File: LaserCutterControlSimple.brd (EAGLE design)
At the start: 75.9 x 53.3 mm, 31 parts, among them J4 FAN, J5 AIR, J6 E-STOP, J7 04-JST-B4B-XH-A, Q1 FDN5630, Q2 FDN5630, U3 R1SE-0505, Y2 POLOLU_A4988, Y3 POLOLU_A4988

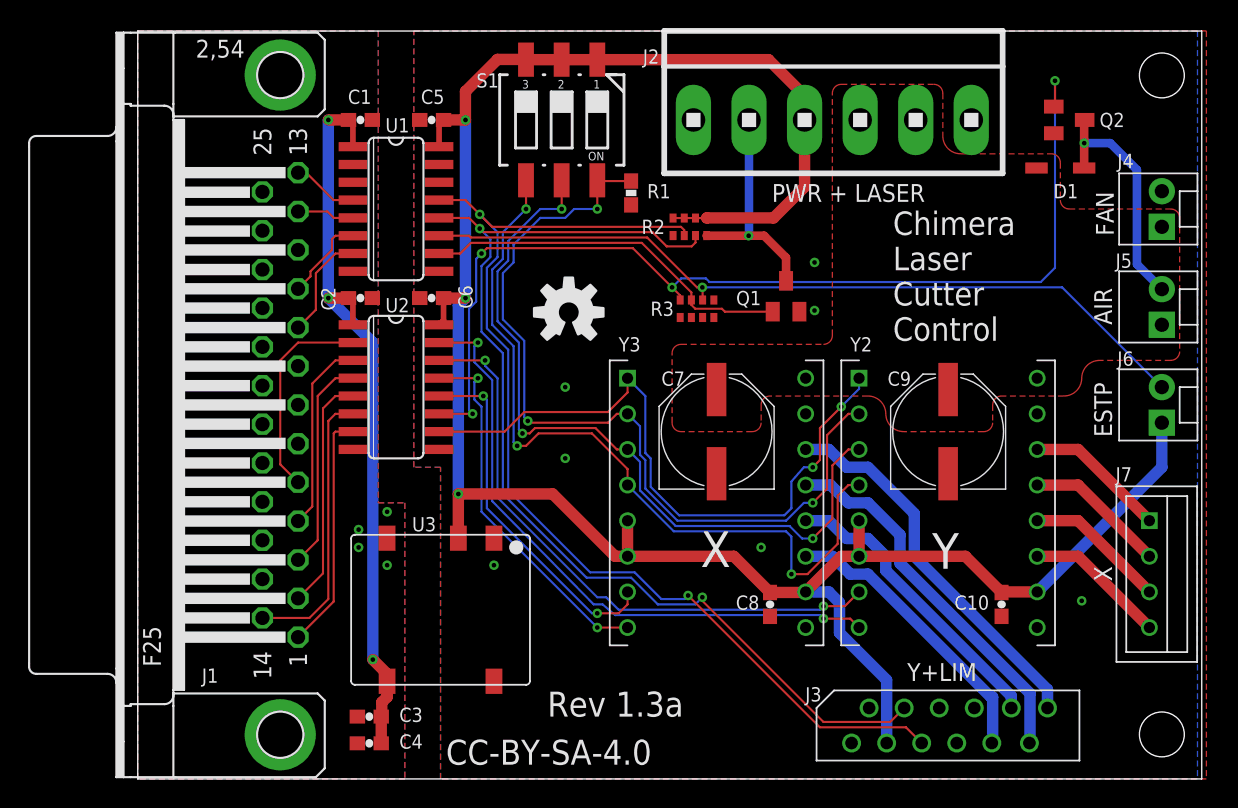
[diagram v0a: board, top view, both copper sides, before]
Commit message: Minor dumb change because it was very early in the morning when I finished the simplified board design. Silk screen and connector change to better match laser cutter connections.
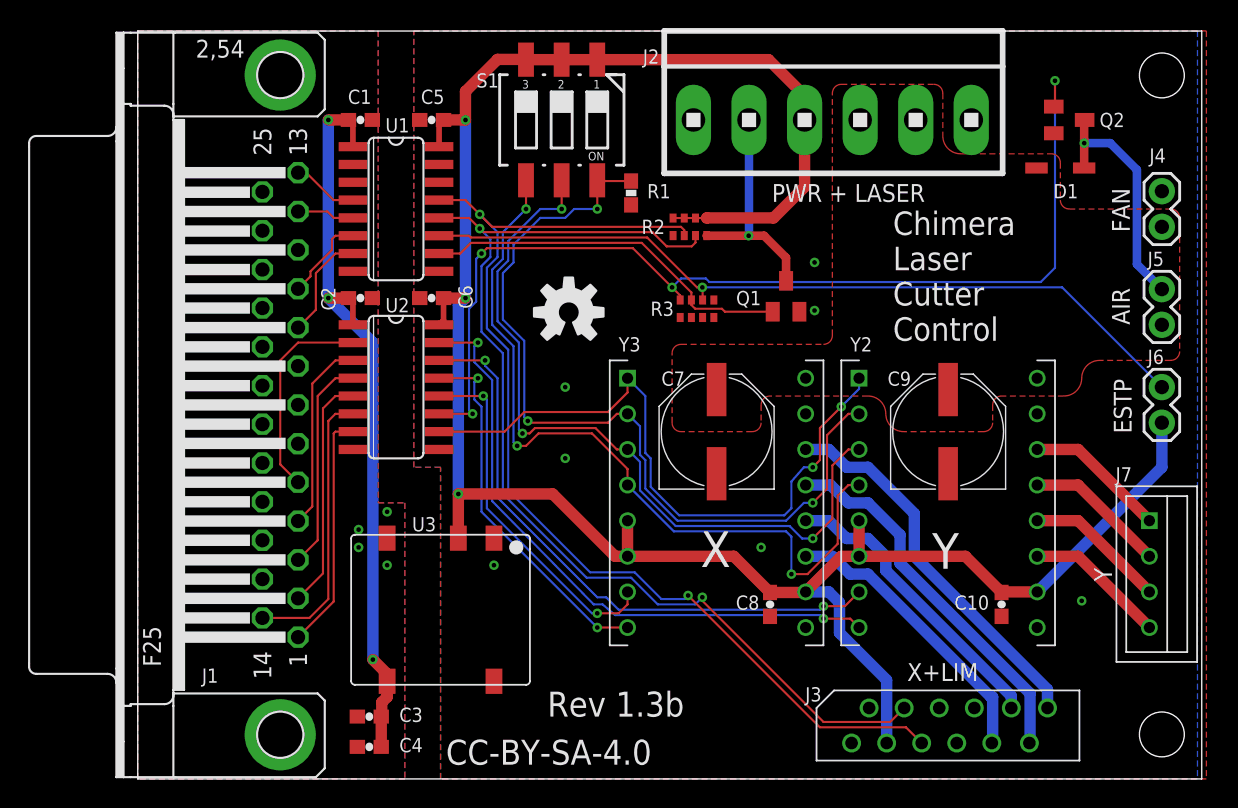
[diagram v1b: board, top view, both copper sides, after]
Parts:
- J4, J5, J6: device SparkFun-Connectors:MOLEX-1X2 -> SparkFun-Connectors:1X02
- moved C4 0.25 mm to (16.5, 2.29)
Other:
- board text added: "Rev 1.3b"
- board text added: "X+LIM"
- board text removed: "Rev 1.3a"
- board text removed: "Y+LIM"
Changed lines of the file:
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@@
 <hole x="73.025" y="50.165" drill="3.2"/>
 <hole x="73.025" y="3.175" drill="3.2"/>
-<text x="69.469" y="32.385" size="1.27" layer="21" font="vector" ratio="12" rot="R90">AIR</text>
-<text x="69.469" y="24.384" size="1.27" layer="21" font="vector" ratio="12" rot="R90">ESTP</text>
-<text x="69.469" y="14.097" size="1.27" layer="21" font="vector" ratio="12" rot="R90">X</text>
-<text x="69.596" y="38.735" size="1.27" layer="21" font="vector" ratio="12" rot="R90">FAN</text>
-<text x="54.864" y="6.985" size="1.27" layer="21" font="vector" ratio="12">Y+LIM</text>
+<text x="70.739" y="32.385" size="1.27" layer="21" font="vector" ratio="12" rot="R90">AIR</text>
+<text x="70.866" y="24.638" size="1.27" layer="21" font="vector" ratio="12" rot="R90">ESTP</text>
+<text x="69.469" y="14.097" size="1.27" layer="21" font="vector" ratio="12" rot="R90">Y</text>
+<text x="70.739" y="38.989" size="1.27" layer="21" font="vector" ratio="12" rot="R90">FAN</text>
+<text x="54.864" y="6.985" size="1.27" layer="21" font="vector" ratio="12">X+LIM</text>
 <text x="53.848" y="31.242" size="1.6764" layer="21" font="vector" ratio="15">Chimera
 Laser
 Cutter
 Control</text>
-<text x="69.85" y="43.561" size="1.016" layer="21" font="vector" ratio="12">J4</text>
-<text x="69.723" y="36.449" size="1.016" layer="21" font="vector" ratio="12">J5</text>
-<text x="69.85" y="29.464" size="1.016" layer="21" font="vector" ratio="12">J6</text>
+<text x="72.136" y="43.942" size="1.016" layer="21" font="vector" ratio="12">J4</text>
+<text x="72.009" y="36.576" size="1.016" layer="21" font="vector" ratio="12">J5</text>
+<text x="72.009" y="29.591" size="1.016" layer="21" font="vector" ratio="12">J6</text>
 <text x="56.134" y="42.418" size="1.27" layer="21" font="vector" ratio="12" rot="R180">PWR + LASER</text>
 <text x="40.132" y="15.113" size="2.54" layer="21" font="vector" ratio="15">X</text>
 <text x="56.642" y="14.986" size="2.54" layer="21" font="vector" ratio="15">Y</text>
 <text x="21.971" y="1.016" size="1.778" layer="21" font="vector" ratio="12">CC-BY-SA-4.0</text>
-<text x="29.21" y="4.445" size="1.778" layer="21" font="vector" ratio="12">Rev 1.3a</text>
+<text x="29.21" y="4.445" size="1.778" layer="21" font="vector" ratio="12">Rev 1.3b</text>
 </plain>
 <attributes>
@@
 <attribute name="VALUE" x="17.526" y="5.588" size="0.4064" layer="27" font="vector" rot="R180" display="off"/>
 </element>
-<element name="C4" library="SparkFun-Capacitors" package="0603-CAP" value="2.2uF" x="16.51" y="2.54" locked="yes" smashed="yes" rot="R180">
-<attribute name="PROD_ID" value="CAP-07886" x="16.51" y="2.54" size="1.778" layer="27" rot="R180" display="off"/>
-<attribute name="NAME" x="20.32" y="3.175" size="1.016" layer="25" font="vector" ratio="12" rot="R180"/>
-<attribute name="VALUE" x="17.526" y="3.683" size="0.4064" layer="27" font="vector" rot="R180" display="off"/>
+<element name="C4" library="SparkFun-Capacitors" package="0603-CAP" value="2.2uF" x="16.51" y="2.286" smashed="yes" rot="R180">
+<attribute name="PROD_ID" value="CAP-07886" x="16.51" y="2.286" size="1.778" layer="27" rot="R180" display="off"/>
+<attribute name="NAME" x="20.32" y="2.921" size="1.016" layer="25" font="vector" ratio="12" rot="R180"/>
+<attribute name="VALUE" x="17.526" y="3.429" size="0.4064" layer="27" font="vector" rot="R180" display="off"/>
 </element>
 <element name="C5" library="SparkFun-Capacitors" package="0603-CAP" value="1nF" x="20.955" y="46.99" locked="yes" smashed="yes" rot="R180">
@@
 <attribute name="VALUE" x="-3.81" y="18.288" size="1.778" layer="27" ratio="10" rot="R90"/>
 </element>
-<element name="J4" library="SparkFun-Connectors" package="MOLEX-1X2" value="FAN" x="73.025" y="39.37" locked="yes" smashed="yes" rot="R90"/>
-<element name="J6" library="SparkFun-Connectors" package="MOLEX-1X2" value="E-STOP" x="73.025" y="25.4" locked="yes" smashed="yes" rot="R90"/>
+<element name="J4" library="SparkFun-Connectors" package="1X02" value="FAN" x="73.025" y="39.37" locked="yes" smashed="yes" rot="R90"/>
+<element name="J6" library="SparkFun-Connectors" package="1X02" value="E-STOP" x="73.025" y="25.4" locked="yes" smashed="yes" rot="R90"/>
 <element name="J3" library="con-amp-te" package="12P" value="" x="57.15" y="3.81" locked="yes" smashed="yes">
 <attribute name="OC_NEWARK" value="unknown" x="57.15" y="3.81" size="1.778" layer="27" display="off"/>
@@
 <attribute name="VALUE" x="38.1351" y="51.3408" size="1.27" layer="27"/>
 </element>
-<element name="J5" library="SparkFun-Connectors" package="MOLEX-1X2" value="AIR" x="73.025" y="32.385" locked="yes" smashed="yes" rot="R90"/>
+<element name="J5" library="SparkFun-Connectors" package="1X02" value="AIR" x="73.025" y="32.385" locked="yes" smashed="yes" rot="R90"/>
 <element name="LOGO1" library="SparkFun-Aesthetics" package="OSHW-LOGO-M" value="OSHW-LOGOM" x="30.734" y="33.274"/>
 <element name="Q2" library="Fairchild_By_element14_Batch_1" package="SOT23" value="FDN5630" x="66.421" y="46.99" locked="yes" smashed="yes" rot="R270">
@@
 <element name="U1" library="silicon-labs" package="SO16" value="" x="18.415" y="40.64" locked="yes" smashed="yes" rot="R270">
 <attribute name="VALUE" x="17.78" y="44.704" size="1.27" layer="27" ratio="10" rot="R270"/>
-<attribute name="NAME" x="17.653" y="46.101" size="1.016" layer="25" font="vector"/>
+<attribute name="NAME" x="17.653" y="46.101" size="1.016" layer="25" font="vector" ratio="12"/>
 </element>
 <element name="U2" library="silicon-labs" package="SO16" value="" x="18.415" y="27.94" locked="yes" smashed="yes" rot="R270">
@@
 <wire x1="17.399" y1="5.461" x2="17.399" y2="4.484" width="0.8128" layer="1"/>
 <wire x1="17.399" y1="4.484" x2="17.36" y2="4.445" width="0.8128" layer="1"/>
-<wire x1="17.36" y1="4.445" x2="17.36" y2="2.54" width="0.8128" layer="1"/>
+<wire x1="17.36" y1="4.445" x2="17.36" y2="2.286" width="0.8128" layer="1"/>
 <wire x1="17.78" y1="6.965" x2="17.78" y2="7.493" width="0.8128" layer="1"/>
 <wire x1="17.78" y1="7.493" x2="16.764" y2="8.509" width="0.8128" layer="1"/>

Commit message: More tweaks to 1.3-1 and 1.3b, some repositioning and swapping of parts for layout, now that I've seen what the inside of the laser cutter looks like. Added pinouts for X and Y limits to the simple board, and just now realize I might have problems with the digital isolators being one way only...
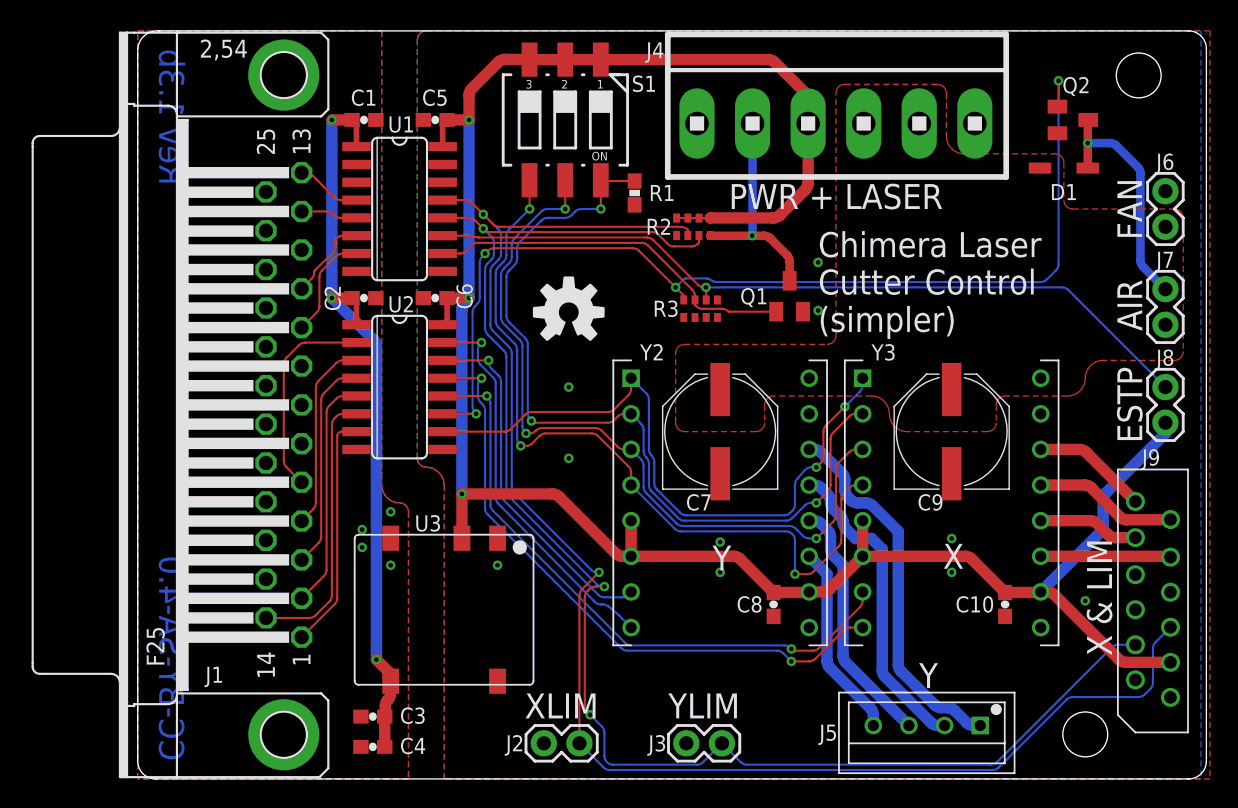
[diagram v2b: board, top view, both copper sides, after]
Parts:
- added J8: E-STOP, SparkFun-Connectors:1X02
- added J9: (no value), con-amp-te:12P
- J2: value (none) -> XLIM; device con-amp:1X6MTA -> SparkFun-Connectors:1X02
- J3: value (none) -> YLIM; device con-amp-te:12P -> SparkFun-Connectors:1X02
- J4: value FAN -> (none); device SparkFun-Connectors:1X02 -> con-amp:1X6MTA
- J5: value AIR -> 04-JST-B4B-XH-A; device SparkFun-Connectors:1X02 -> con-jst-xh:B4B-XH
- J6: value E-STOP -> FAN
- J7: value 04-JST-B4B-XH-A -> AIR; device con-jst-xh:B4B-XH -> SparkFun-Connectors:1X02
- moved J2 49.0 mm to (29.0, 2.54)
- moved J5 33.1 mm to (56.3, 3.81), turned to 180 degrees
- moved J4 24.4 mm to (49.8, 46.7), turned to 0 degrees
- moved J3 18.1 mm to (39.1, 2.54)
- moved J7 17.8 mm to (73.3, 32.4), turned to 90 degrees
- moved Y3 16.8 mm to (58.0, 19.7)
- moved Y2 16.3 mm to (41.5, 19.7)
- moved J6 14.0 mm to (73.3, 39.4)
- moved C7 0.25 mm to (41.5, 24.8)
- moved C9 0.25 mm to (58.0, 24.8)
- moved D1 0.25 mm to (66.0, 43.6)
- moved R2 0.25 mm to (39.6, 39.4)
- moved C1 0.25 mm to (16.1, 47.0)
- moved C2 0.25 mm to (16.1, 34.3)
- moved C5 0.25 mm to (21.2, 47.0)
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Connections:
- net CNC_24V: now also J4.2, J6.1, J7.1; no longer J2.2, J4.1, J5.1
- net CNC_5V: now also J4.4, J8.1, J9.3; no longer J2.4, J3.3, J6.1
- net CNC_GND: now also J3.1, J4.1, J4.6, J6.2, J9.6; no longer J2.6, J3.6, J4.2
- net ESTOP_ISO: now also J8.2; no longer J6.2
- net LASER: now also J4.5; no longer J2.5
- net N$8: now also J7.2; no longer J5.2
- net XLIM_ISO: now also J2.2, J9.5; no longer J3.5
- net X_A+: now also J9.12; no longer J3.12
- net X_A-: now also J9.11; no longer J3.11
- net X_B+: now also J9.10; no longer J3.10
- net X_B-: now also J9.9; no longer J3.9
- net YLIM_ISO: now also J3.2, J9.4; no longer J3.4
- net Y_A+: now also J5.P$1; no longer J7.P$1
- net Y_A-: now also J5.P$2; no longer J7.P$2
- net Y_B+: now also J5.P$3; no longer J7.P$3
- net Y_B-: now also J5.P$4; no longer J7.P$4
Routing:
- net XLIM_ISO: track 77.1 -> 109.5 mm
- net YLIM_ISO: track 76.2 -> 105.5 mm, vias 2 -> 3
- net X_A+: track 27.4 -> 8.25 mm
- net XSTP_ISO: track 25.5 -> 44.0 mm
- net XDIR_ISO: track 26.4 -> 44.6 mm
- net YSTP_ISO: track 43.0 -> 25.6 mm, vias 2 -> 1
- net YDIR_ISO: track 44.6 -> 27.9 mm, vias 2 -> 1
- net X_A-: track 26.9 -> 10.2 mm
- net Y_A+: track 10.1 -> 26.5 mm
- net X_B+: track 21.3 -> 7.17 mm
- net Y_A-: track 10.1 -> 22.4 mm
- net X_B-: track 20.8 -> 9.28 mm
- net Y_B+: track 10.1 -> 17.8 mm
- net Y_B-: track 10.1 -> 13.9 mm
- net CNC_5V: track 164.1 -> 160.6 mm
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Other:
- board size 75.9 x 53.3 mm -> 76.2 x 53.3 mm
- board text added: "Chimera Laser Cutter Control (simpler)"
- board text added: "J7"
- board text added: "J8"
- board text added: "Randy Hall"
- board text added: "X & LIM"
- board text removed: "Chimera Laser Cutter Control"
- board text removed: "J4"
- board text removed: "J5"
- board text removed: "X+LIM"
